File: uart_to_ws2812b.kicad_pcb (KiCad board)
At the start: 2 copper layers, 70 x 70 mm, 64 parts, among them J1 USB_B_Micro, J2 Prog. Header, J3 Power Header, J4 UART, J5 I2C, J6 SPI, J8 Conn_01x03, J9 Conn_01x03, Q1 Q_NPN_BEC, SW1 SW_Push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

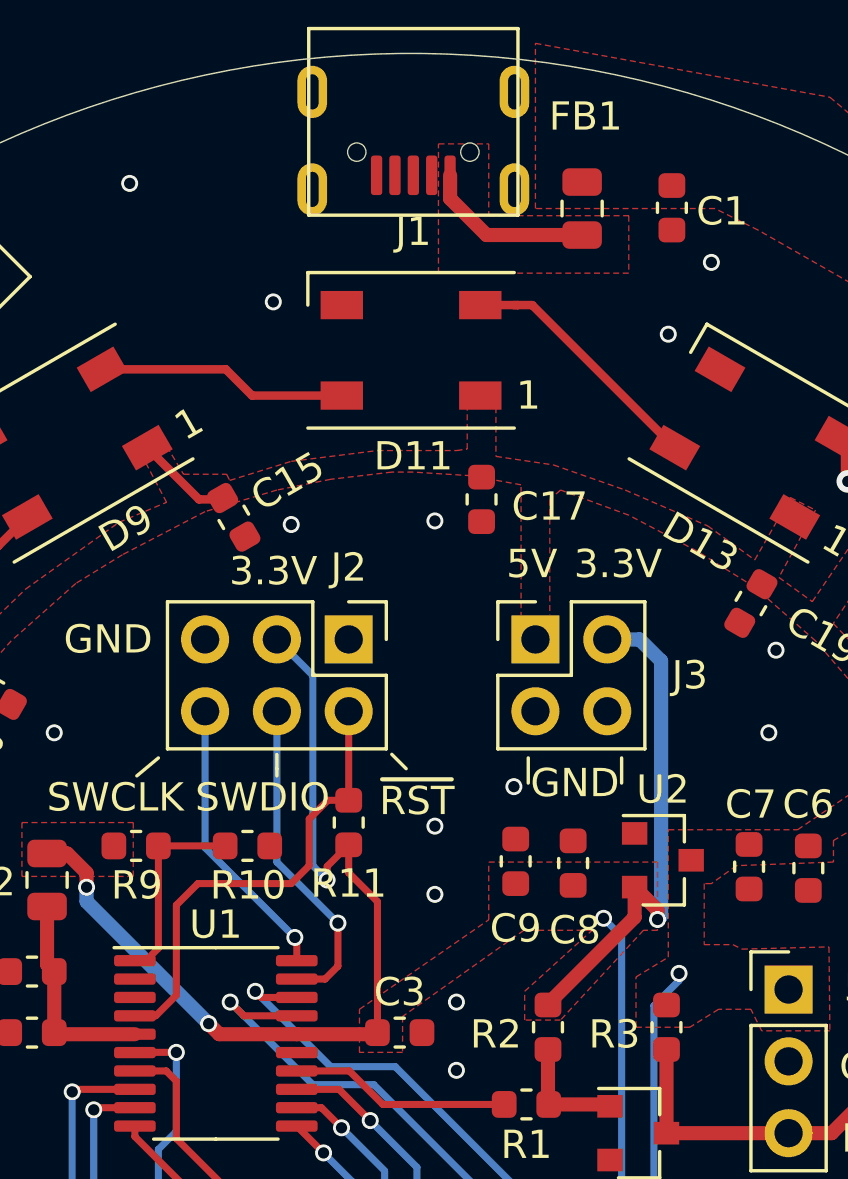
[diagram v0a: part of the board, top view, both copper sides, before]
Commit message: Shorted D+ and D- to indicate charging mode
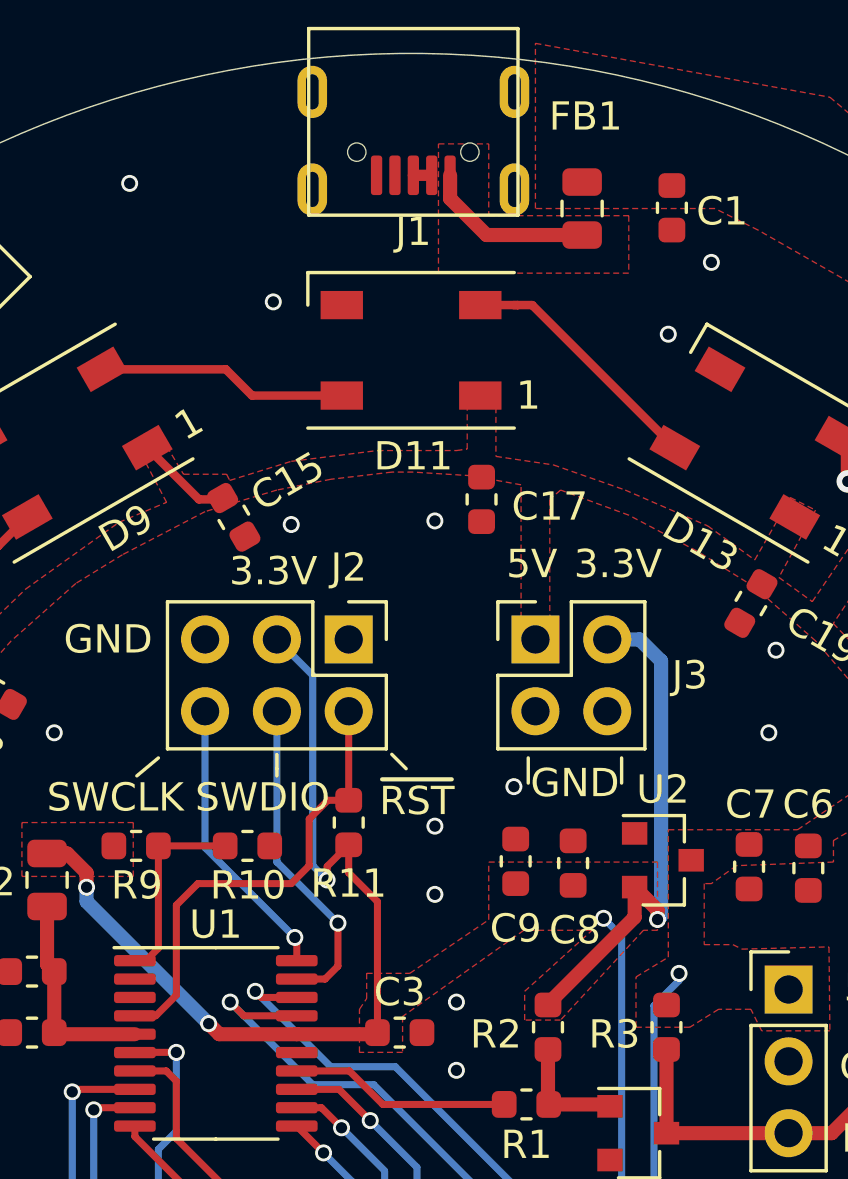
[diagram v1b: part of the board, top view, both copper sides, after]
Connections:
- J1 pad 3: Net-(J1-Pad3) -> Net-(J1-Pad2)
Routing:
- net Net-(J1-Pad2): track 0.00 -> 0.65 mm

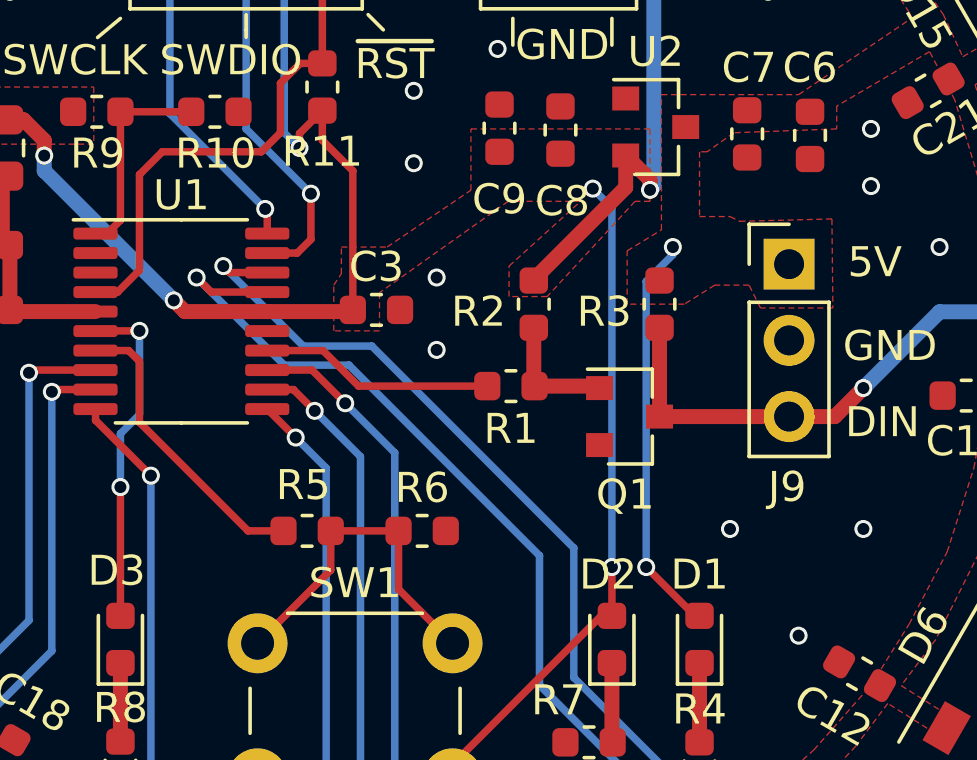
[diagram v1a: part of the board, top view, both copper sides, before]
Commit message: Changed to a level shifting IC for the LED data logic
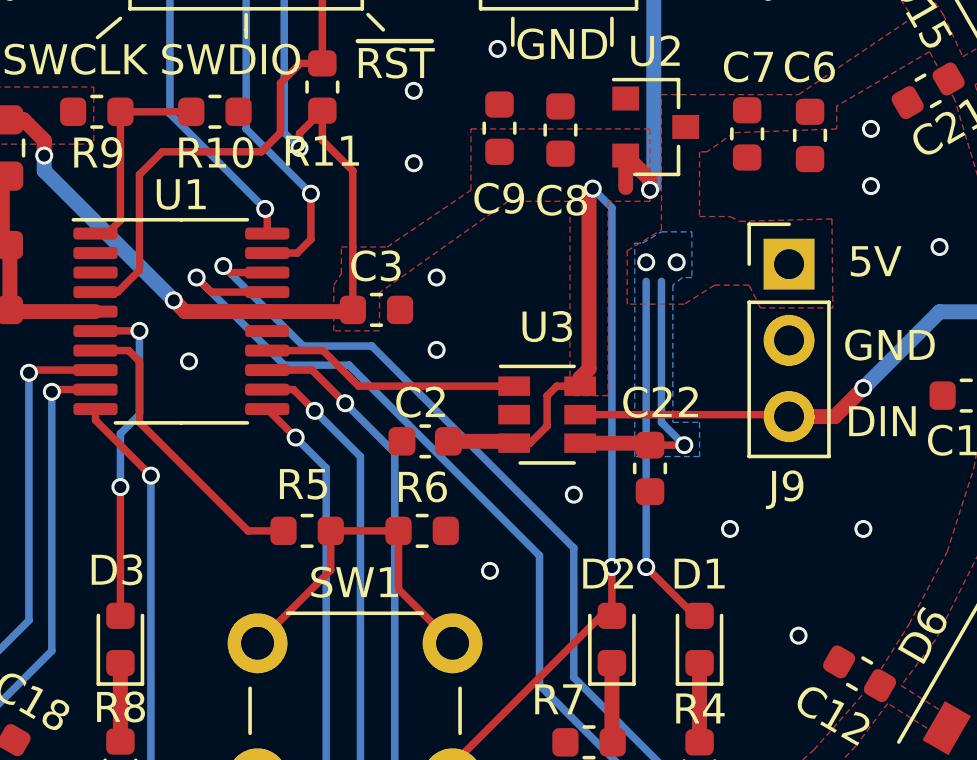
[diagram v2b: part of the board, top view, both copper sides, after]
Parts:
- removed Q1: Q_NPN_BEC, Package_TO_SOT_SMD:SOT-23
- removed R1: 1kR, Resistor_SMD:R_0603_1608Metric
- removed R2, R3: 10kR, Resistor_SMD:R_0603_1608Metric
- added C2: 0.1uF, Capacitor_SMD:C_0603_1608Metric, F.Cu at (141.2, 104.0)
- added C22: 0.1uF, Capacitor_SMD:C_0603_1608Metric, F.Cu at (148.7, 104.9)
- added U3: PI4ULS5V201TAEX, Package_TO_SOT_SMD:SOT-23-6, F.Cu at (145.3, 103.1)
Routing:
- net +3V3: track 80.1 -> 88.2 mm
- net +5V: track 20.4 -> 28.2 mm, vias 2 -> 4
- net /Data_B: track 4.15 -> 0.00 mm
- net /3.3V_Data_Out: track 7.83 -> 8.72 mm
- net GND: vias 45 -> 48
- added copper zone on B.Cu, net +5V

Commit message: Updated component information with more detail
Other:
- rule pad_to_mask_clearance: 0.05 -> 0
